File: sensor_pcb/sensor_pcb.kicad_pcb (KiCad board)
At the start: 2 copper layers, 64 x 111.4 mm, 58 parts, among them J1 AVR-ISP-6, J3 Arc, J4 Arc, Q1 AO3401A, Q2 AO3401A, U1 MCP1700-3302E_SOT23, U2 HIH6131-021-001, U3 ATmega328P-AU, Y1 8 MHz

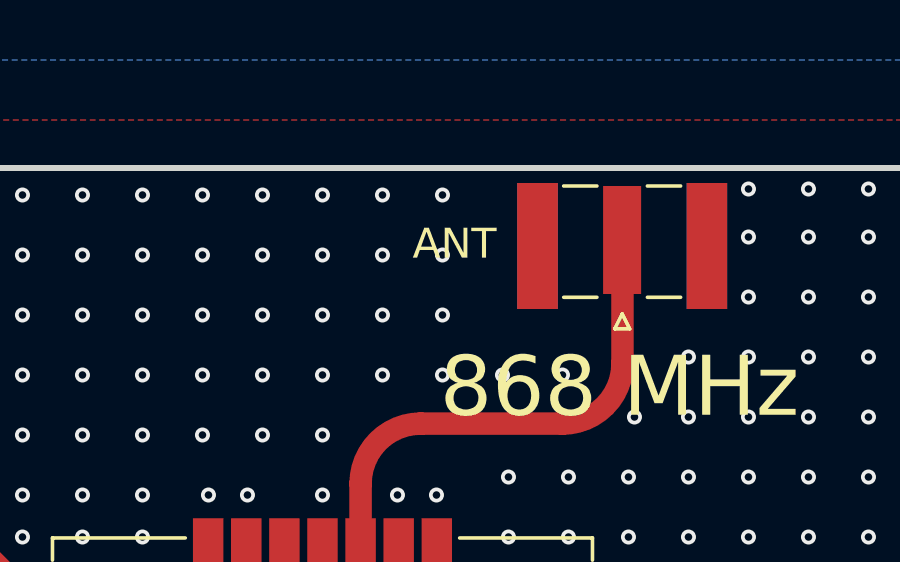
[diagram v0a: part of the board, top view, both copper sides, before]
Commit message: Added sensor case
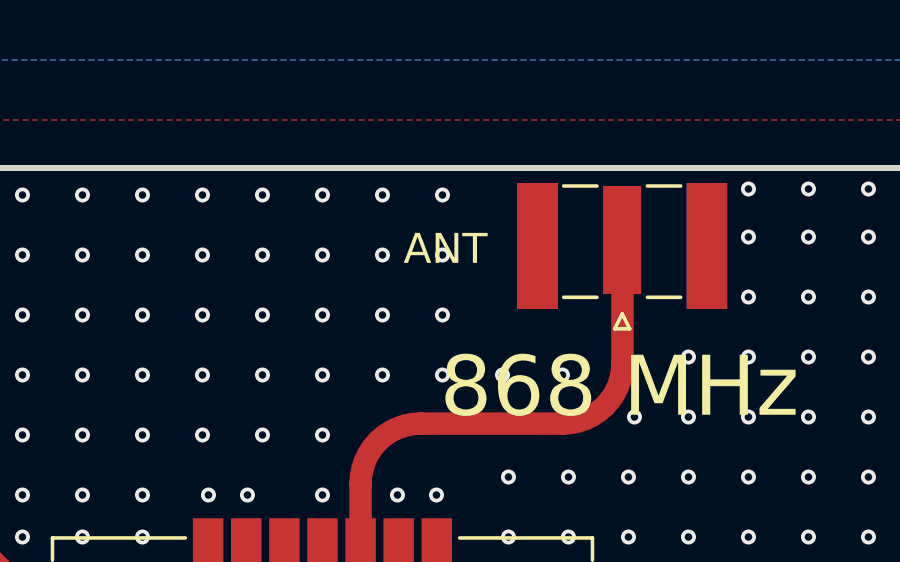
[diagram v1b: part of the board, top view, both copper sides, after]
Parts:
- ANT: footprint Connector_Coaxial:SMA_Samtec_SMA-J-P-X-ST-EM1_EdgeMount -> sensor_pcb:SMA_Samtec_SMA-J-P-X-ST-EM1_EdgeMount
